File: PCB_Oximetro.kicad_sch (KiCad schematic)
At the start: 14 parts, among them J1 Conn_01x05, J2 Conn_01x08, J3 USB_B_Micro, SW1 SW_Push, U3 LM1117MP-3.3, U5 ESP32-DEVKIT-V1

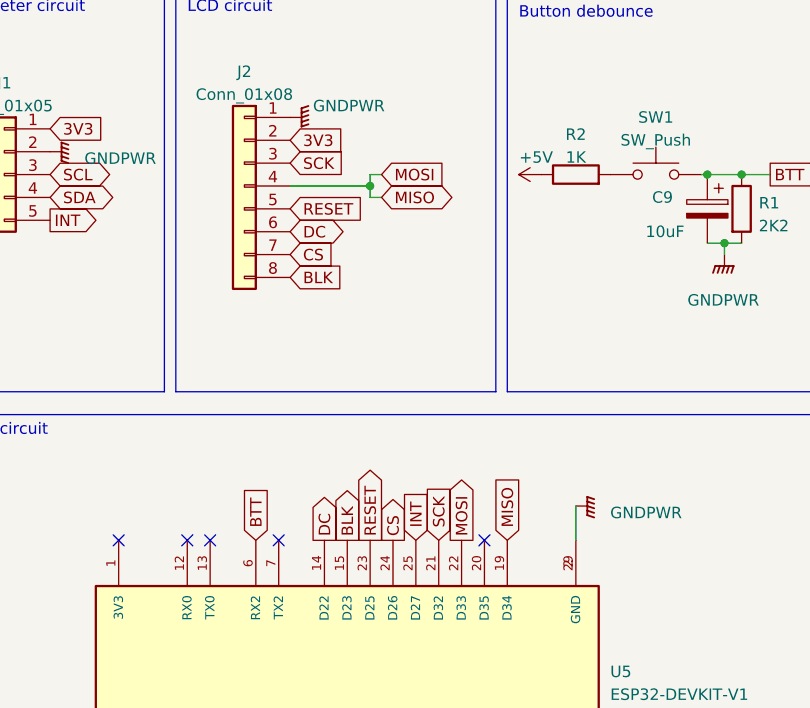
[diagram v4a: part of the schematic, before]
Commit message: Update MISO
MISO Removed for compatibility
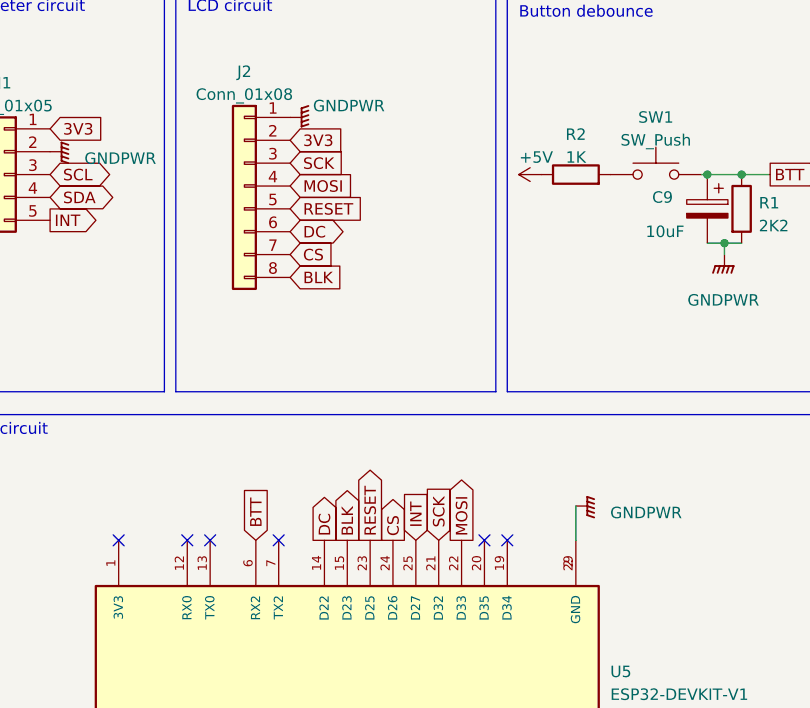
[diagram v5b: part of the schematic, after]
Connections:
- net MISO renamed MOSI
- net MOSI: no longer U5.19 (D34)
- no-connect marks 19 -> 20
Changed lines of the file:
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@@
   (junction (at 97.79 38.1) (diameter 0) (color 0 0 0 0)
-  )
-  (junction (at 63.5 77.47) (diameter 0) (color 0 0 0 0)
   )
   (junction (at 100.965 76.2) (diameter 0) (color 0 0 0 0)
@@
   (no_connect (at 66.04 147.32))
   (no_connect (at 35.56 116.84))
-  (wire (pts (xy 64.77 76.2) (xy 63.5 76.2))
-    (stroke (width 0) (type default))
-  )
+  (no_connect (at 78.74 116.84))
   (wire (pts (xy 67.31 29.21) (xy 76.2 29.21))
     (stroke (width 0) (type default))
@@
     (stroke (width 0) (type default))
   )
-  (wire (pts (xy 63.5 78.74) (xy 63.5 77.47))
-    (stroke (width 0) (type default))
-  )
   (wire (pts (xy 67.31 38.1) (xy 76.2 38.1))
     (stroke (width 0) (type default))
@@
     (stroke (width 0) (type default))
   )
-  (wire (pts (xy 63.5 77.47) (xy 54.61 77.47))
-    (stroke (width 0) (type default))
-  )
   (wire (pts (xy 102.87 83.82) (xy 104.775 83.82))
     (stroke (width 0) (type default))
@@
     (stroke (width 0) (type default))
   )
-  (wire (pts (xy 64.77 78.74) (xy 63.5 78.74))
-    (stroke (width 0) (type default))
-  )
-  (wire (pts (xy 63.5 76.2) (xy 63.5 77.47))
-    (stroke (width 0) (type default))
-  )
   (wire (pts (xy 97.79 36.83) (xy 97.79 38.1))
     (stroke (width 0) (type default))
@@
     (effects (font (size 1.27 1.27)) (justify left bottom))
   )
-  (global_label "MISO" (shape bidirectional) (at 64.77 78.74 0) (fields_autoplaced)
-    (effects (font (size 1.27 1.27)) (justify left))
-    (property "Intersheetrefs" "${INTERSHEET_REFS}" (at 73.3833 78.74 0)
-      (effects (font (size 1.27 1.27)) (justify left) hide)
-    )
-  )
   (global_label "RESET" (shape input) (at 54.61 80.01 0) (fields_autoplaced)
     (effects (font (size 1.27 1.27)) (justify left))
@@
     )
   )
-  (global_label "MISO" (shape input) (at 78.74 116.84 90) (fields_autoplaced)
-    (effects (font (size 1.27 1.27)) (justify left))
-    (property "Intersheetrefs" "${INTERSHEET_REFS}" (at 78.74 109.338 90)
-      (effects (font (size 1.27 1.27)) (justify left) hide)
-    )
-  )
   (global_label "MOSI" (shape output) (at 73.66 116.84 90) (fields_autoplaced)
     (effects (font (size 1.27 1.27)) (justify left))
@@
     )
   )
-  (global_label "MOSI" (shape input) (at 64.77 76.2 0) (fields_autoplaced)
-    (effects (font (size 1.27 1.27)) (justify left))
-    (property "Intersheetrefs" "${INTERSHEET_REFS}" (at 72.272 76.2 0)
-      (effects (font (size 1.27 1.27)) (justify left) hide)
-    )
+  (global_label "MOSI" (shape input) (at 54.61 77.47 0) (fields_autoplaced)
+    (effects (font (size 1.27 1.27)) (justify left))
+    (property "Intersheetrefs" "${INTERSHEET_REFS}" (at 62.112 77.47 0)
+      (effects (font (size 1.27 1.27)) (justify left) hide)
+    )

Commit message: Capacitor size change
Changed capacitor smd 1206 to 0805 because of availibility
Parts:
- C1, C3: footprint Capacitor_SMD:C_1206_3216Metric -> Capacitor_SMD:C_0805_2012Metric
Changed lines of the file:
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@@
       (effects (font (size 1.27 1.27)) (justify left))
     )
-    (property "Footprint" "Capacitor_SMD:C_1206_3216Metric" (at 75.2348 36.83 0)
+    (property "Footprint" "Capacitor_SMD:C_0805_2012Metric" (at 75.2348 36.83 0)
       (effects (font (size 1.27 1.27)) hide)
     )
@@
       (effects (font (size 1.27 1.27)) (justify left))
     )
-    (property "Footprint" "Capacitor_SMD:C_1206_3216Metric" (at 98.7552 36.83 0)
-      (effects (font (size 1.27 1.27)) hide)
-    )
+    (property "Footprint" "Capacitor_SMD:C_0805_2012Metric" (at 98.7552 36.83 0)
+      (effects (font (size 1.27 1.27)) hide)
+    )

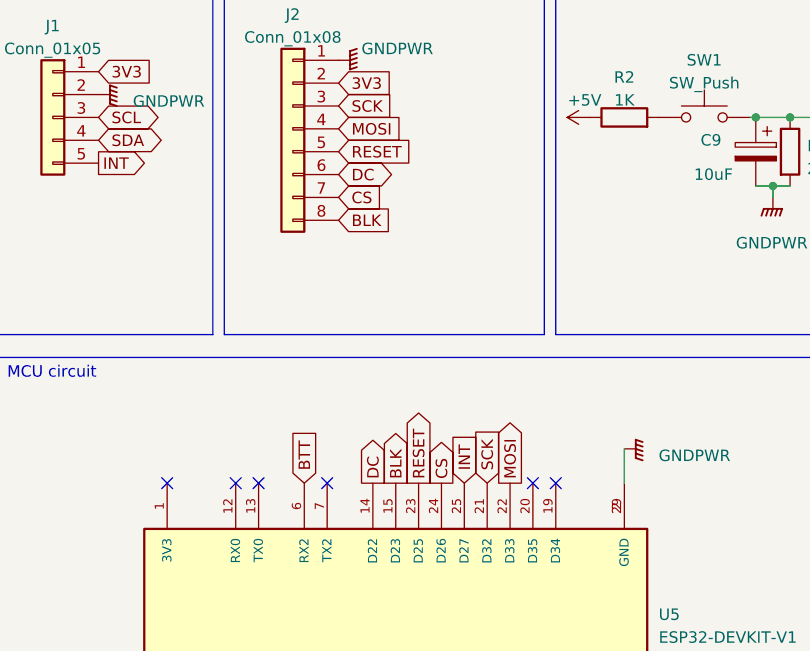
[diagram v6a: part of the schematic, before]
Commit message: BLK Pin update
Changed BLK pin to make the PCB 1 only front layer
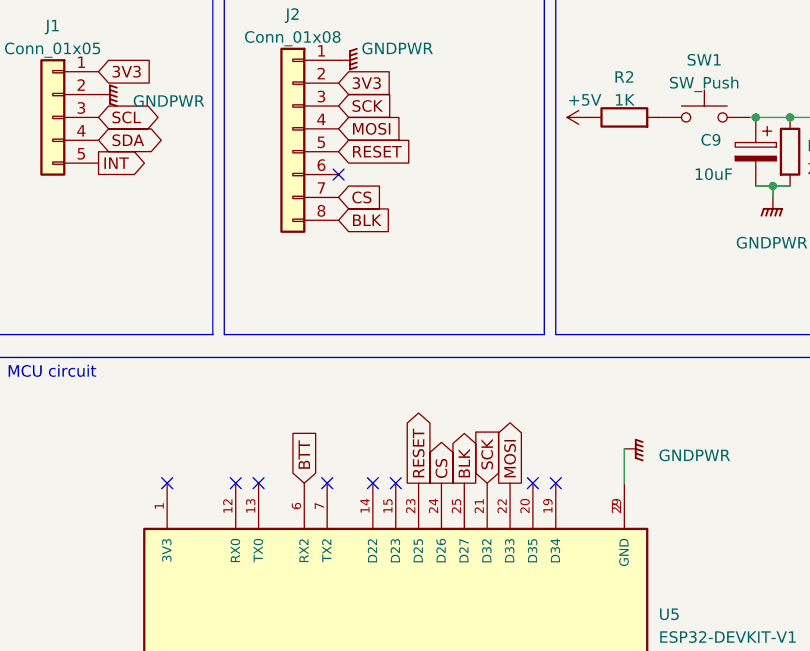
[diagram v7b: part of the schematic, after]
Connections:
- net BLK: now also U5.25 (D27); no longer U5.15 (D23)
- net INT: no longer U5.25 (D27)
- net DC: no longer names the net of U5.14 (D22)
- net DC: no longer J2.6 (Pin_6)
- no-connect marks 20 -> 23
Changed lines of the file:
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@@
   (no_connect (at 53.34 116.84))
   (no_connect (at 43.18 116.84))
+  (no_connect (at 58.42 116.84))
   (no_connect (at 73.66 147.32))
   (no_connect (at 43.18 147.32))
+  (no_connect (at 66.04 147.32))
+  (no_connect (at 60.96 116.84))
   (no_connect (at 30.48 39.37))
   (no_connect (at 30.48 34.29))
@@
   (no_connect (at 38.1 147.32))
   (no_connect (at 81.28 147.32))
+  (no_connect (at 54.61 82.55))
   (no_connect (at 58.42 147.32))
   (no_connect (at 63.5 147.32))
   (no_connect (at 30.48 36.83))
-  (no_connect (at 66.04 147.32))
   (no_connect (at 35.56 116.84))
   (no_connect (at 78.74 116.84))
@@
     (effects (font (size 1.27 1.27)) (justify left))
     (property "Intersheetrefs" "${INTERSHEET_REFS}" (at 73.66 109.338 90)
-      (effects (font (size 1.27 1.27)) (justify left) hide)
-    )
-  )
-  (global_label "DC" (shape output) (at 58.42 116.84 90) (fields_autoplaced)
-    (effects (font (size 1.27 1.27)) (justify left))
-    (property "Intersheetrefs" "${INTERSHEET_REFS}" (at 58.42 111.3942 90)
-      (effects (font (size 1.27 1.27)) (justify left) hide)
-    )
-  )
-  (global_label "DC" (shape bidirectional) (at 54.61 82.55 0) (fields_autoplaced)
-    (effects (font (size 1.27 1.27)) (justify left))
-    (property "Intersheetrefs" "${INTERSHEET_REFS}" (at 61.1671 82.55 0)
       (effects (font (size 1.27 1.27)) (justify left) hide)
     )
@@
     )
   )
-  (global_label "BLK" (shape output) (at 60.96 116.84 90) (fields_autoplaced)
-    (effects (font (size 1.27 1.27)) (justify left))
-    (property "Intersheetrefs" "${INTERSHEET_REFS}" (at 60.96 110.3661 90)
-      (effects (font (size 1.27 1.27)) (justify left) hide)
-    )
-  )
-  (global_label "INT" (shape input) (at 68.58 116.84 90) (fields_autoplaced)
-    (effects (font (size 1.27 1.27)) (justify left))
-    (property "Intersheetrefs" "${INTERSHEET_REFS}" (at 68.58 111.0313 90)
-      (effects (font (size 1.27 1.27)) (justify left) hide)
-    )
+  (global_label "BLK" (shape output) (at 68.58 116.84 90) (fields_autoplaced)
+    (effects (font (size 1.27 1.27)) (justify left))
+    (property "Intersheetrefs" "${INTERSHEET_REFS}" (at 68.58 110.3661 90)
+      (effects (font (size 1.27 1.27)) (justify left) hide)
+    )

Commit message: Update PCB
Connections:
- net DC: now reaches U5.14 (D22)
- net DC: now also J2.6 (Pin_6)
- no-connect marks 23 -> 21
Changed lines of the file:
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@@
   (no_connect (at 53.34 116.84))
   (no_connect (at 43.18 116.84))
-  (no_connect (at 58.42 116.84))
   (no_connect (at 73.66 147.32))
   (no_connect (at 43.18 147.32))
@@
   (no_connect (at 38.1 147.32))
   (no_connect (at 81.28 147.32))
-  (no_connect (at 54.61 82.55))
   (no_connect (at 58.42 147.32))
   (no_connect (at 63.5 147.32))
@@
     (effects (font (size 1.27 1.27)) (justify left bottom))
   )
+  (global_label "DC" (shape input) (at 54.61 82.55 0) (fields_autoplaced)
+    (effects (font (size 1.27 1.27)) (justify left))
+    (property "Intersheetrefs" "${INTERSHEET_REFS}" (at 60.0558 82.55 0)
+      (effects (font (size 1.27 1.27)) (justify left) hide)
+    )
+  )
   (global_label "RESET" (shape input) (at 54.61 80.01 0) (fields_autoplaced)
     (effects (font (size 1.27 1.27)) (justify left))
@@
       (effects (font (size 1.27 1.27)) (justify left) hide)
     )
+  )
+  (global_label "DC" (shape input) (at 58.42 116.84 90) (fields_autoplaced)
+    (effects (font (size 1.27 1.27)) (justify left))
+    (property "Intersheetrefs" "${INTERSHEET_REFS}" (at 58.42 111.3942 90)
+      (effects (font (size 1.27 1.27)) (justify left) hide)
+    )
